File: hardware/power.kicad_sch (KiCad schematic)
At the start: 8 parts, among them J1 Eurorack_Power, U1 MP1584 (3.3V), U2 MP1584 (5V)

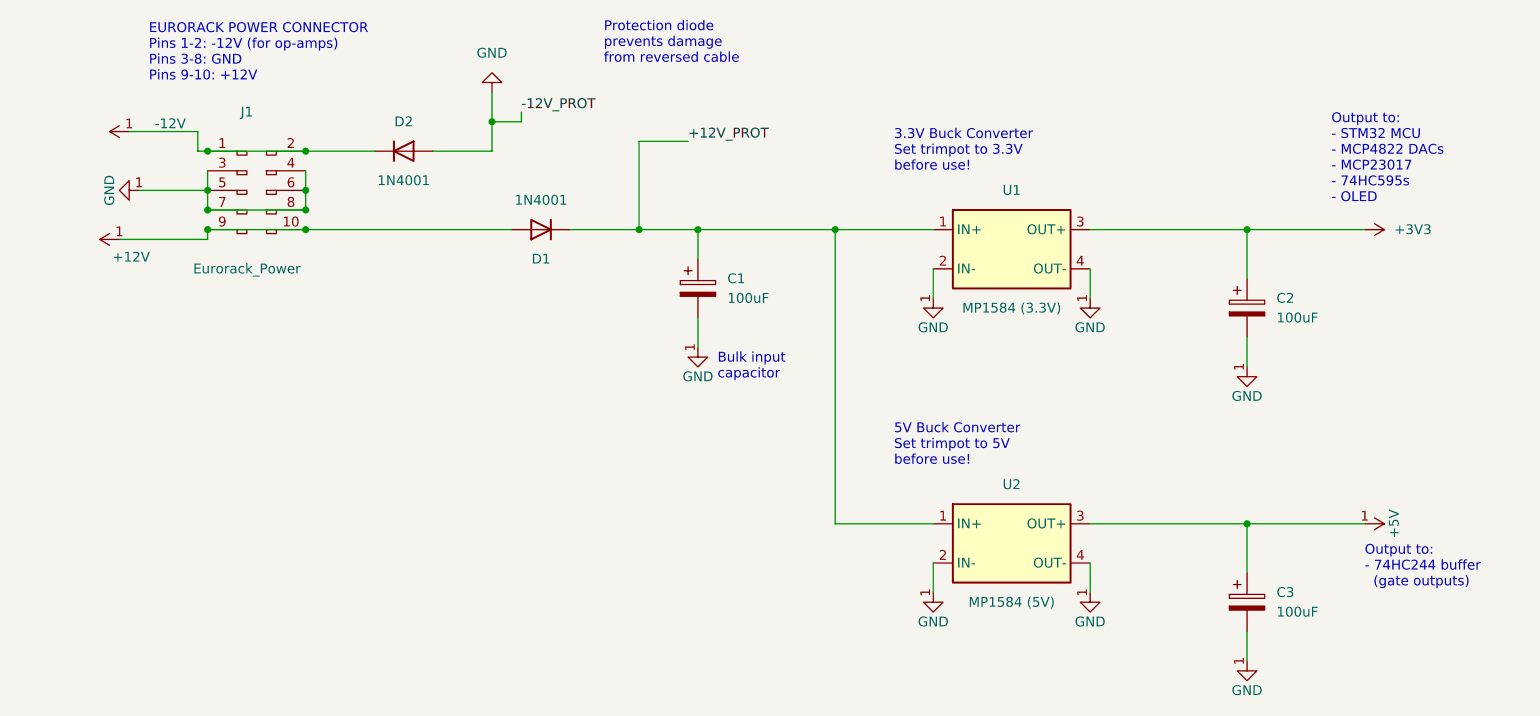
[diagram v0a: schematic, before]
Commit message: Complete hierarchical schematic sheets and fix wiring
- Complete encoder_leds sheet with MAX7219 + 64 LEDs
- Complete ui_leds sheet with MAX7219 + 45 LEDs
- Complete buttons sheet with MCP23017 + 40 buttons
- Complete display sheet with OLED I2C connector
- Complete pots sheet with 3 potentiometers
- Complete encoders sheet with 8 rotary encoders on MCP23017
- Fix inputs sheet hierarchical labels (CLK_IN, RST_IN, SCENE_CV_IN)
- Update MCU sheet with ADC hierarchical labels
- Update root sheet with hierarchical pin connections
- Various ERC fixes and wiring corrections

Co-Authored-By: Claude Opus 4.5 <noreply@anthropic.com>
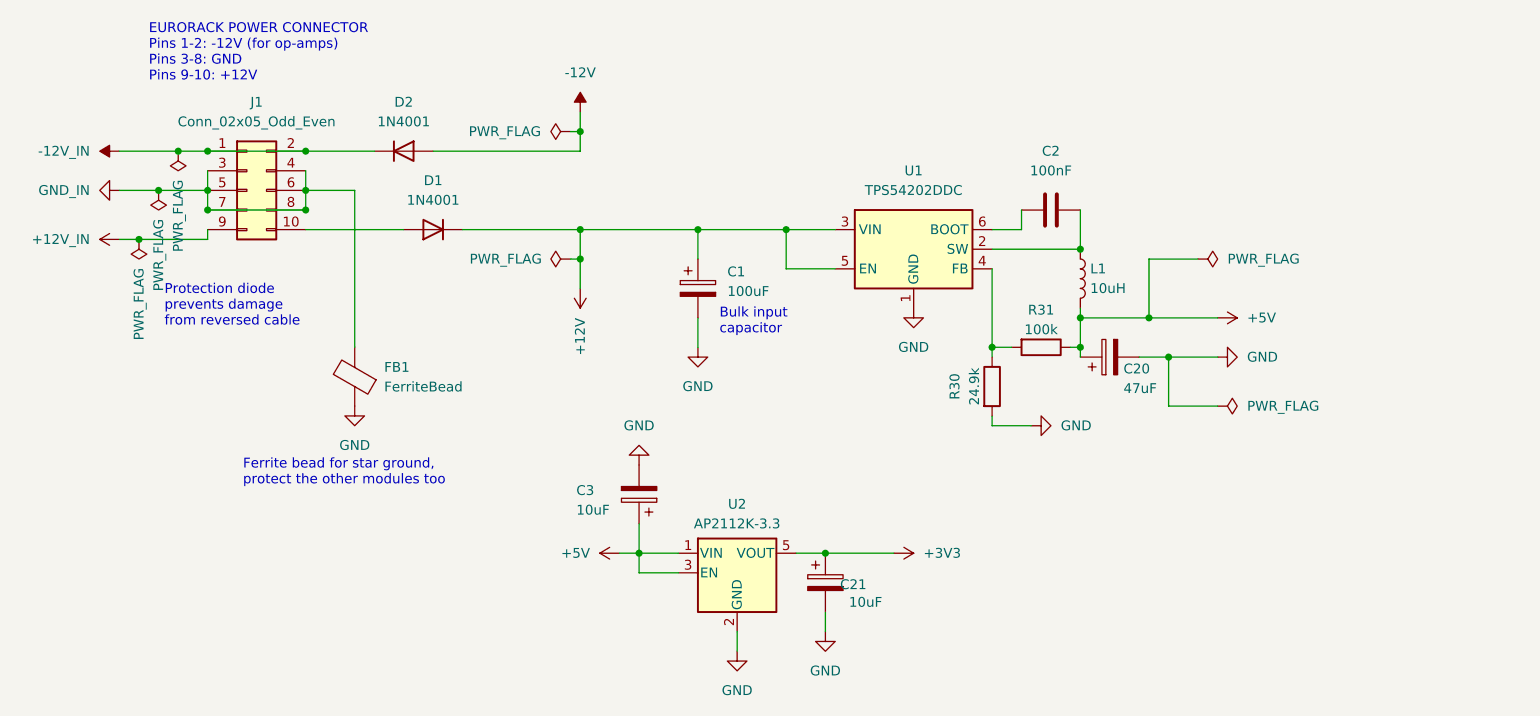
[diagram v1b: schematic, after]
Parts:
- removed C1, C2, C3: 100uF, Capacitor_THT:CP_Radial_D8.0mm_P3.50mm, symbol Device:CP
- removed D1, D2: 1N4001, Diode_THT:D_DO-41_SOD81_P10.16mm_Horizontal, symbol Device:D
- removed J1: Eurorack_Power, Connector_IDC:IDC-Header_2x05_P2.54mm_Vertical, symbol Connector:Conn_02x05_Odd_Even
- removed U1: MP1584 (3.3V), Connector_PinHeader_2.54mm:PinHeader_1x04_P2.54mm_Vertical, symbol Regulator_Switching:MP1584_Module
- removed U2: MP1584 (5V), Connector_PinHeader_2.54mm:PinHeader_1x04_P2.54mm_Vertical, symbol Regulator_Switching:MP1584_Module
- added C1: 100uF, symbol Device:C_Polarized
- added C2: 100nF, symbol Device:C
- added C20: 47uF, symbol Device:C_Polarized
- added C21, C3: 10uF, symbol Device:C_Polarized
- added D1, D2: 1N4001, Diode_THT:D_DO-41_SOD81_P10.16mm_Horizontal, symbol Diode:1N4001
- added FB1: FerriteBead, Inductor_SMD:L_Eaton_MCL2012V1, symbol Device:FerriteBead
- added J1: Conn_02x05_Odd_Even, Connector_IDC:IDC-Header_2x05_P2.54mm_Vertical, symbol Connector_Generic:Conn_02x05_Odd_Even
- added L1: 10uH, symbol Device:L
- added R30: 24.9k, symbol Device:R
- added R31: 100k, symbol Device:R
- added U1: TPS54202DDC, Package_TO_SOT_SMD:SOT-23-6, symbol Regulator_Switching:TPS54202DDC
- added U2: AP2112K-3.3, Package_TO_SOT_SMD:SOT-23-5, symbol Regulator_Linear:AP2112K-3.3
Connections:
- net +12V: now also C1.1, D1.1 (K), U1.3 (VIN), U1.5 (EN)
- net +3V3: now also C21.1, U2.5 (VOUT)
- net +5V: now also C20.1, C3.1, L1.2, R31.1, U2.1 (VIN), U2.3 (EN)
- net -12V: now also D2.2 (A)
- net GND: now also C1.2, C20.2, C21.2, C3.2, FB1.1, R30.2, U1.1 (GND), U2.2 (GND)
- new net: D1.2 (A), J1.10 (Pin_10)
- new net: C2.1, U1.6 (BOOT)
- new net: C2.2, L1.1, U1.2 (SW)
- new net: R30.1, R31.2, U1.4 (FB)
- new net +12V_IN: J1.9 (Pin_9)
- new net -12V_IN: D2.1 (K), J1.1 (Pin_1), J1.2 (Pin_2)
- new net GND_IN: FB1.2, J1.3 (Pin_3), J1.4 (Pin_4), J1.5 (Pin_5), J1.6 (Pin_6), J1.7 (Pin_7), J1.8 (Pin_8)
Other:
- note added: "Ferrite bead for star ground, protect the other modules too"
- note removed: "3.3V Buck Converter Set trimpot to 3.3V before use!"
- note removed: "5V Buck Converter Set trimpot to 5V before use!"
- note removed: "Output to: - 74HC244 buffer (gate outputs)"
- note removed: "Output to: - STM32 MCU - MCP4822 DACs - MCP23017 - 74HC595s - OLED"

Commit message: Assign footprints to all schematic components
SMD footprints assigned:
- Capacitors: 0402 (20pF), 0603 (100nF), 0805 (10uF), 1206 (47uF, 100uF)
- Resistors: 0603
- LEDs: 0201
- MAX7219: SOIC-24W
- ULN2003: SOIC-16
- Switches: TL3342 tactile
- Connectors: JST PH, pin headers

Also removes accidentally committed autosave files.

Co-Authored-By: Claude Opus 4.5 <noreply@anthropic.com>
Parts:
- C1, C20: footprint (none) -> Capacitor_SMD:C_1206_3216Metric
- C2: footprint (none) -> Capacitor_SMD:C_0603_1608Metric
- C21, C3: footprint (none) -> Capacitor_SMD:C_0805_2012Metric
- L1: footprint (none) -> Inductor_SMD:L_0201_0603Metric_Pad0.64x0.40mm_HandSolder
- R30, R31: footprint (none) -> Resistor_SMD:R_0201_0603Metric_Pad0.64x0.40mm_HandSolder
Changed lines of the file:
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@@
 			)
 		)
-		(property "Footprint" ""
+		(property "Footprint" "Capacitor_SMD:C_0603_1608Metric"
 			(at 200.66 75.2348 0)
 			(effects
@@
 			)
 		)
-		(property "Footprint" ""
+		(property "Footprint" "Capacitor_SMD:C_0805_2012Metric"
 			(at 142.5448 109.22 0)
 			(effects
@@
 			)
 		)
-		(property "Footprint" ""
+		(property "Footprint" "Inductor_SMD:L_0201_0603Metric_Pad0.64x0.40mm_HandSolder"
 			(at 200.66 85.09 0)
 			(effects
@@
 			)
 		)
-		(property "Footprint" ""
+		(property "Footprint" "Capacitor_SMD:C_0805_2012Metric"
 			(at 168.6052 128.27 0)
 			(effects
@@
 			)
 		)
-		(property "Footprint" ""
+		(property "Footprint" "Capacitor_SMD:C_1206_3216Metric"
 			(at 208.28 94.2848 0)
 			(effects
@@
 			)
 		)
-		(property "Footprint" ""
+		(property "Footprint" "Resistor_SMD:R_0201_0603Metric_Pad0.64x0.40mm_HandSolder"
 			(at 187.452 99.06 90)
 			(effects
@@
 			)
 		)
-		(property "Footprint" ""
+		(property "Footprint" "Capacitor_SMD:C_1206_3216Metric"
 			(at 152.0952 90.17 0)
 			(effects
@@
 			)
 		)
-		(property "Footprint" ""
+		(property "Footprint" "Resistor_SMD:R_0201_0603Metric_Pad0.64x0.40mm_HandSolder"
 			(at 195.58 92.202 90)
 			(effects
